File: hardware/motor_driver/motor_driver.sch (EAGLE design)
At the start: 7 parts

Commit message: updating motor driver design 30/07/15
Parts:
- added R1, R2, R3: 10k, adafruit:R-US_R0805
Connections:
- new net !FAULT: R2.1, U$7.!FAULT
- new net !OCTW: R1.1, U$7.!OCTW
- new net 5V: R1.2, R2.2
- new net DTC: R3.2, U$7.DTC
- new net EN_GATE: U$7.EN_GATE
- new net GND: R3.1
- new net N$10: U$7.INH_A
- new net N$11: U$7.INL_A
- new net N$12: U$7.INH_B
- new net N$13: U$7.INL_B
- new net N$14: U$7.INH_C
- new net N$15: U$7.INL_C
- new net N$16: U$7.PVDD2
- new net N$17: U$7.PVDD2(2)
- new net N$18: U$7.VSENSE
- new net N$19: U$7.BST_BK
- new net N$20: U$7.PH1
- new net N$21: U$7.PH2
- new net N$22: U$7.EN_BUCK
- new net N$23: U$7.PWRGD
- new net N$24: U$7.SS_TR
- new net N$25: U$7.RT_CLK
- new net N$26: U$7.COMP
- new net N$27: U$7.CP1
- new net N$28: U$7.CP2
- new net N$29: U$7.SO1
- new net N$30: U$7.SO2
- new net N$31: U$7.SP2
- new net N$32: U$7.SN2
- new net N$33: U$7.DC_CAL
- new net N$34: U$7.REF
- new net N$35: U$7.SP1
- new net N$36: U$7.SN1
- new net N$37: U$7.SL_C
- new net N$38: U$7.GL_C
- new net N$39: U$7.SH_C
- new net N$40: U$7.GH_C
- new net N$41: U$7.BST_C
- new net N$42: U$7.SL_B
- new net N$43: U$7.GL_B
- new net N$44: U$7.SH_B
- new net N$45: U$7.GH_B
- new net N$46: U$7.BST_B
- new net N$47: U$7.SL_A
- new net N$48: U$7.GL_A
- new net N$49: U$7.SA_A
- new net N$5: U$7.M_PWM
- new net N$50: U$7.GH_A
- new net N$51: U$7.BST_A
- new net N$52: U$7.GND
- new net N$53: U$7.AGND
- new net N$54: U$7.DVDD
- new net N$55: U$7.AVDD
- new net N$56: U$7.GVDD
- new net N$57: U$7.PVDD1
- new net N$6: U$7.M_OC
- new net N$7: U$7.GAIN
- new net N$8: U$7.OC_ADJ
- new net N$9: U$7.BIAS

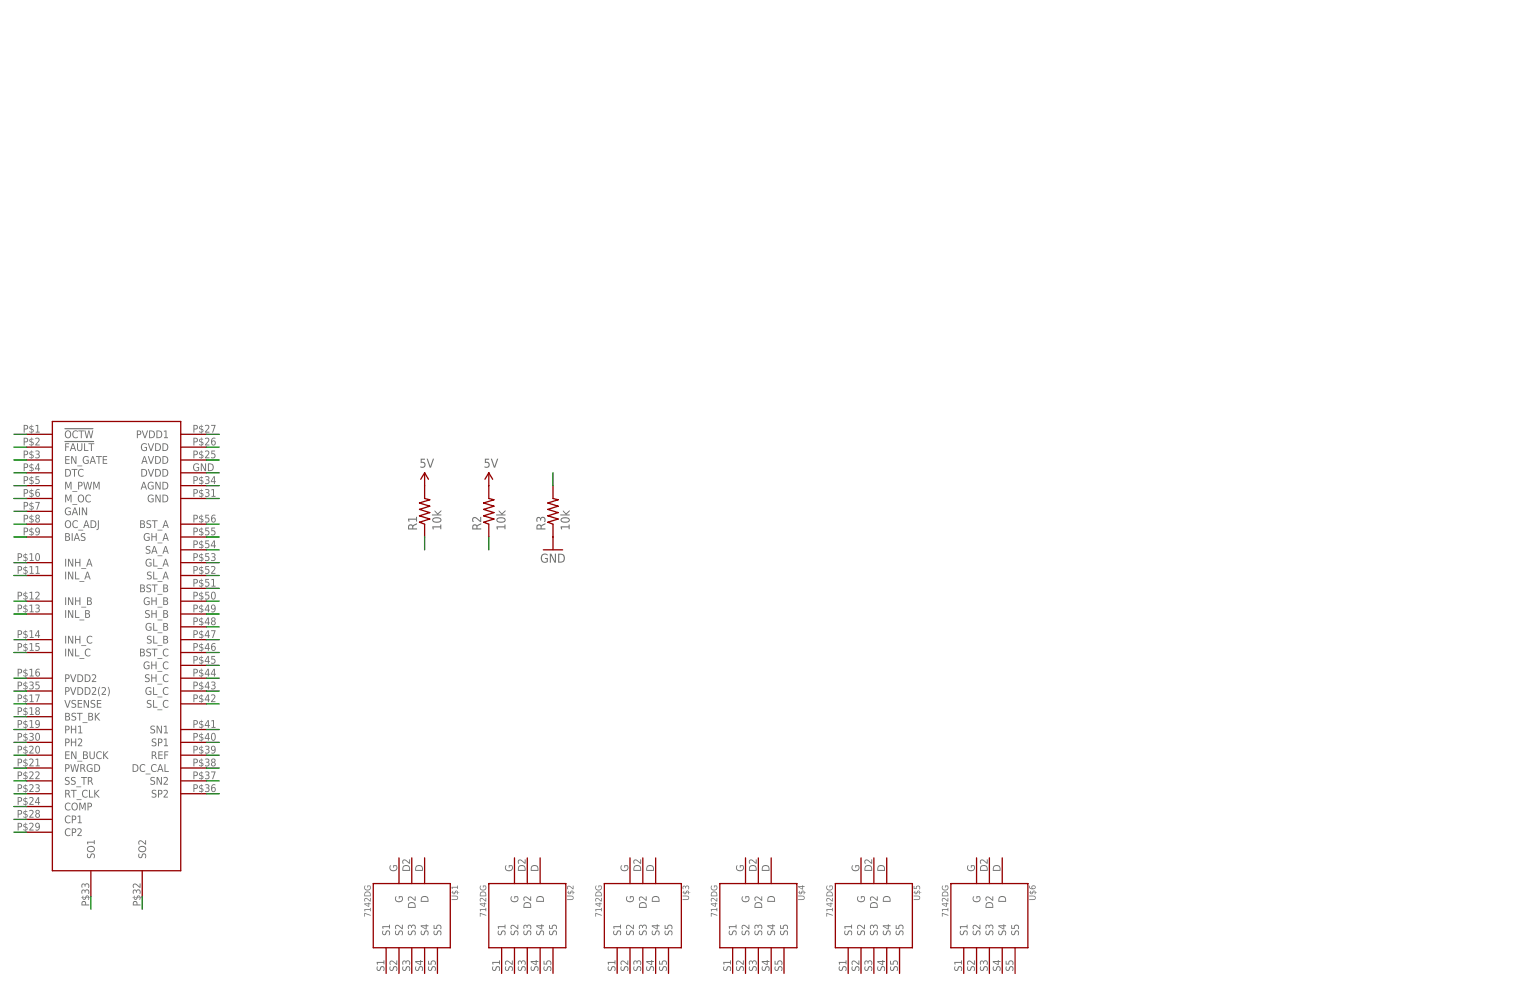
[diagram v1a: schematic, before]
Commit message: Updated motor controller schematic, driver  almost done but components (caps, ind, res) packages still need to be spec'd out
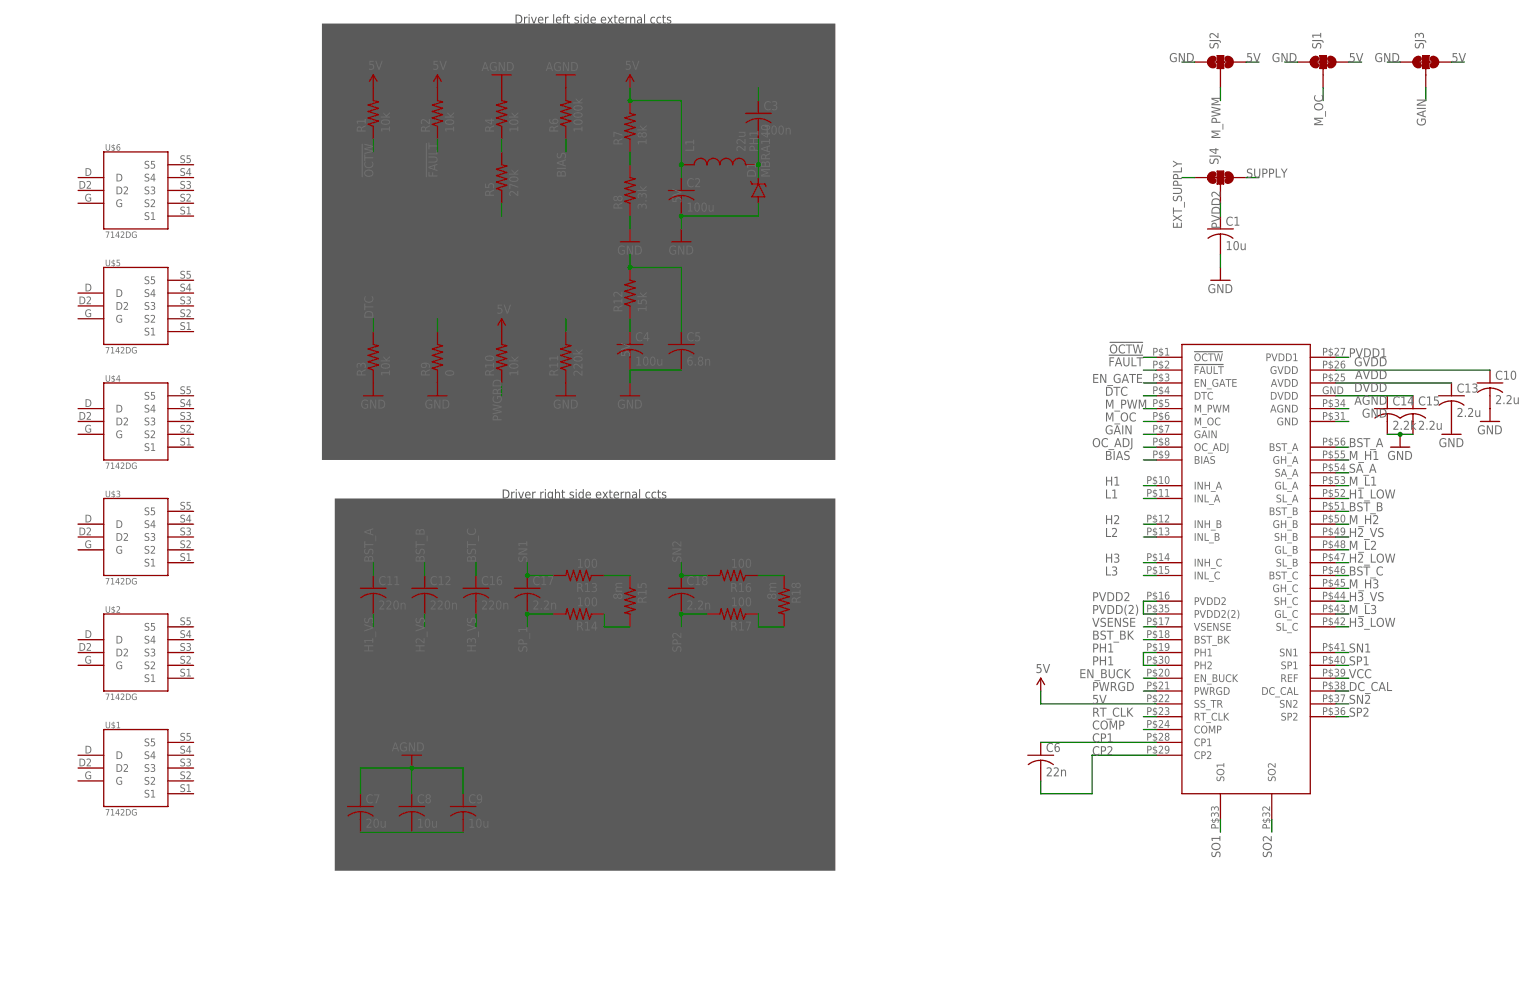
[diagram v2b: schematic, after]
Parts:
- added C1, C8, C9: 10u, adafruit:C-USC1206
- added C10, C13, C15: 2.2u, adafruit:C-USC1206
- added C11, C12, C16: 220n, adafruit:C-USC1206
- added C14: 2.2k, adafruit:C-USC1206
- added C17, C18: 2.2n, adafruit:C-USC1206
- added C2, C4: 100u, adafruit:C-USC1206
- added C3: 100n, adafruit:C-USC1206
- added C5: 6.8n, adafruit:C-USC1206
- added C6: 22n, adafruit:C-USC1206
- added C7: 20u, adafruit:C-USC1206
- added D1: MBRA140, SparkFun-DiscreteSemi:MBRA140
- added L1: 22u, SparkFun-Passives:INDUCTOR30OHM,1.8A
- added R10, R4: 10k, adafruit:R-US_R0805
- added R11: 220k, adafruit:R-US_R0805
- added R12: 15k, adafruit:R-US_R0805
- added R13, R14, R16, R17: 100, adafruit:R-US_R0805
- added R15, R18: 8m, adafruit:R-US_R0805
- added R5: 270k, adafruit:R-US_R0805
- added R6: 1000k, adafruit:R-US_R0805
- added R7: 18k, adafruit:R-US_R0805
- added R8: 3.3k, adafruit:R-US_R0805
- added R9: 0, adafruit:R-US_R0805
- added SJ1, SJ2, SJ3, SJ4: (no value), SparkFun-Passives:JUMPER-PAD-3-NC_BY_TRACE
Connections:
- net N$10 renamed H1
- net N$11 renamed L1
- net N$12 renamed H2
- net N$13 renamed L2
- net N$14 renamed H3
- net N$15 renamed L3
- net N$17 renamed PVDD(2)
- net N$23 renamed PWRGD
- net N$29 renamed SO1
- net N$30 renamed SO2
- net N$33 renamed DC_CAL
- net N$34 renamed VCC
- net N$35 renamed SP1
- net N$38 renamed M_L3
- net N$40 renamed M_H3
- net N$42 renamed H2_LOW
- net N$43 renamed M_L2
- net N$45 renamed M_H2
- net N$48 renamed M_L1
- net N$49 renamed SA_A
- net N$50 renamed M_H1
- removed net N$16: U$7.PVDD2
- removed net N$18: U$7.VSENSE
- removed net N$19: U$7.BST_BK
- removed net N$20: U$7.PH1
- removed net N$21: U$7.PH2
- removed net N$22: U$7.EN_BUCK
- removed net N$24: U$7.SS_TR
- removed net N$25: U$7.RT_CLK
- removed net N$26: U$7.COMP
- removed net N$27: U$7.CP1
- removed net N$28: U$7.CP2
- removed net N$31: U$7.SP2
- removed net N$32: U$7.SN2
- removed net N$36: U$7.SN1
- removed net N$37: U$7.SL_C
- removed net N$39: U$7.SH_C
- removed net N$41: U$7.BST_C
- removed net N$44: U$7.SH_B
- removed net N$46: U$7.BST_B
- removed net N$47: U$7.SL_A
- removed net N$5: U$7.M_PWM
- removed net N$51: U$7.BST_A
- removed net N$52: U$7.GND
- removed net N$53: U$7.AGND
- removed net N$54: U$7.DVDD
- removed net N$55: U$7.AVDD
- removed net N$56: U$7.GVDD
- removed net N$57: U$7.PVDD1
- removed net N$6: U$7.M_OC
- removed net N$7: U$7.GAIN
- removed net N$8: U$7.OC_ADJ
- removed net N$9: U$7.BIAS
- new net AGND: C7.1, C8.1, C9.1, R4.2, R6.2, U$7.AGND
- new net AVDD: C13.1, U$7.AVDD
- new net BIAS: R6.1, U$7.BIAS
- new net BST_A: C11.1, U$7.BST_A
- new net BST_B: C12.1, U$7.BST_B
- new net BST_BK: C3.1, U$7.BST_BK
- new net BST_C: C16.1, U$7.BST_C
- new net COMP: C5.1, R12.2, U$7.COMP
- new net CP1: C6.1, U$7.CP1
- new net CP2: C6.2, U$7.CP2
- new net DVDD: C15.1, R4.1, R5.2, U$7.DVDD
- new net EN_BUCK: R9.2, U$7.EN_BUCK
- new net EXT_SUPPLY: SJ4.1
- new net GAIN: SJ3.2, U$7.GAIN
- new net GVDD: C10.1, U$7.GVDD
- new net H1_LOW: R13.1, R15.1, U$7.SL_A
- new net H1_VS: C11.2
- new net H2_VS: C12.2, U$7.SH_B
- new net H3_LOW: R16.1, R18.1, U$7.SL_C
- new net H3_VS: C16.2, U$7.SH_C
- new net M_OC: SJ1.2, U$7.M_OC
- new net M_PWM: SJ2.2, U$7.M_PWM
- new net N$1: R14.1, R15.2
- new net N$2: R17.1, R18.2
- new net OC_ADJ: R5.1, U$7.OC_ADJ
- new net PH1: C3.2, D1.C, L1.2, U$7.PH1, U$7.PH2
- new net PVDD1: C7.2, C9.2, U$7.PVDD1
- new net PVDD2: C1.1, SJ4.2, U$7.PVDD2
- new net PWGRD: R10.1
- new net RT_CLK: R11.2, U$7.RT_CLK
- new net SN1: C17.1, R13.2, U$7.SN1
- new net SN2: C18.1, R16.2, U$7.SN2
- new net SP2: C18.2, R17.2, U$7.SP2
- new net SP_1: C17.2, R14.2
- new net SUPPLY: SJ4.3
- new net VSENSE: R7.1, R8.2, U$7.VSENSE
- net 5V: now also C2.1, C4.1, L1.1, R10.2, R12.1, R7.2, SJ1.3, SJ2.3, SJ3.3, U$7.SS_TR
- net GND: now also C1.2, C10.2, C13.2, C14.2, C15.2, C2.2, C4.2, C5.2, D1.A, R11.1, R8.1, R9.1, SJ1.1, SJ2.1, SJ3.1, U$7.GND
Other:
- note added: "Driver left side external ccts"
- note added: "Driver right side external ccts"
- moved on the sheet: R1, R2, R3, U$1, U$2, U$3, U$4, U$5, U$6

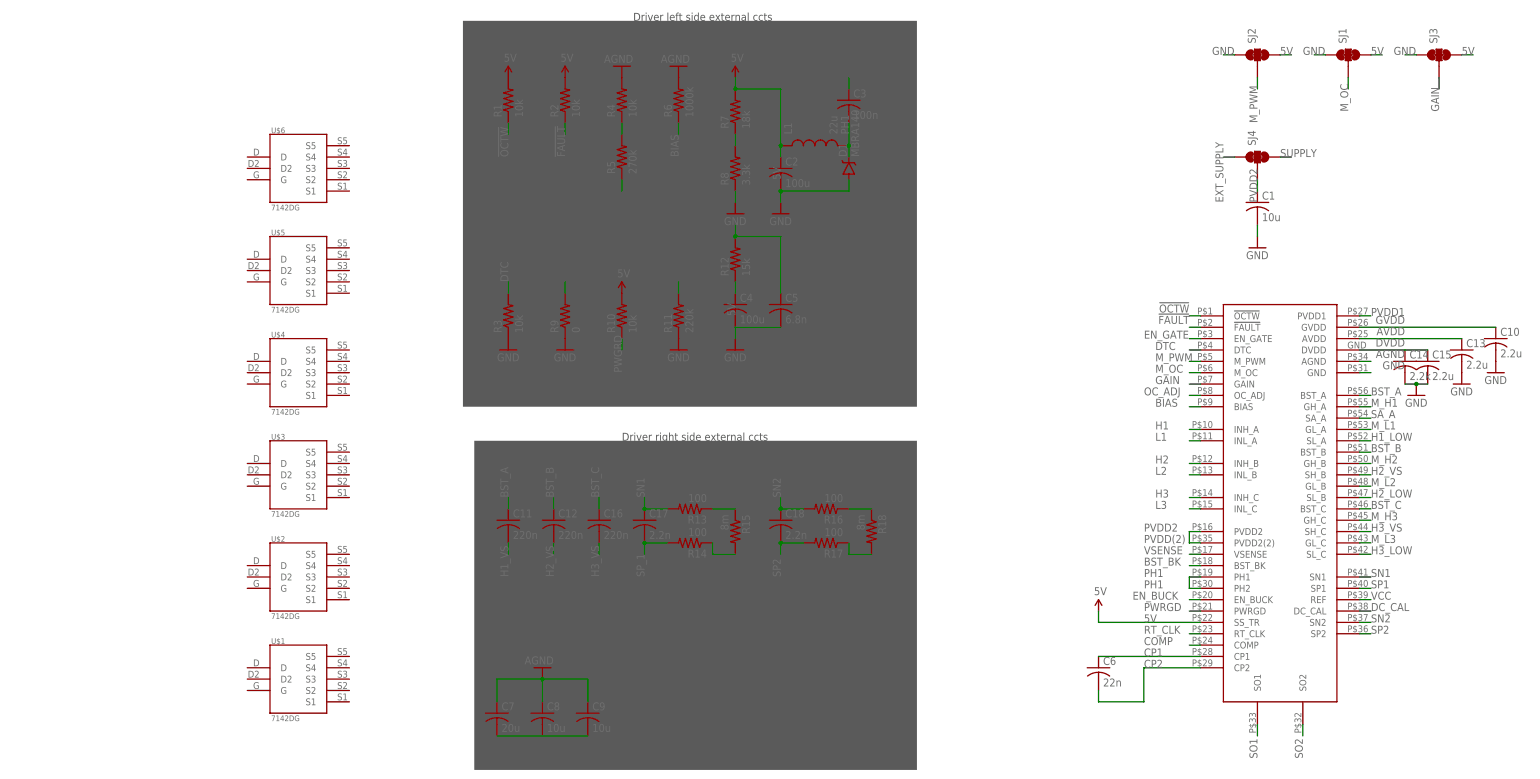
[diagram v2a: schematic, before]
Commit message: Finished driver and MOSFET's external connections. Package choices still need to be reviewed
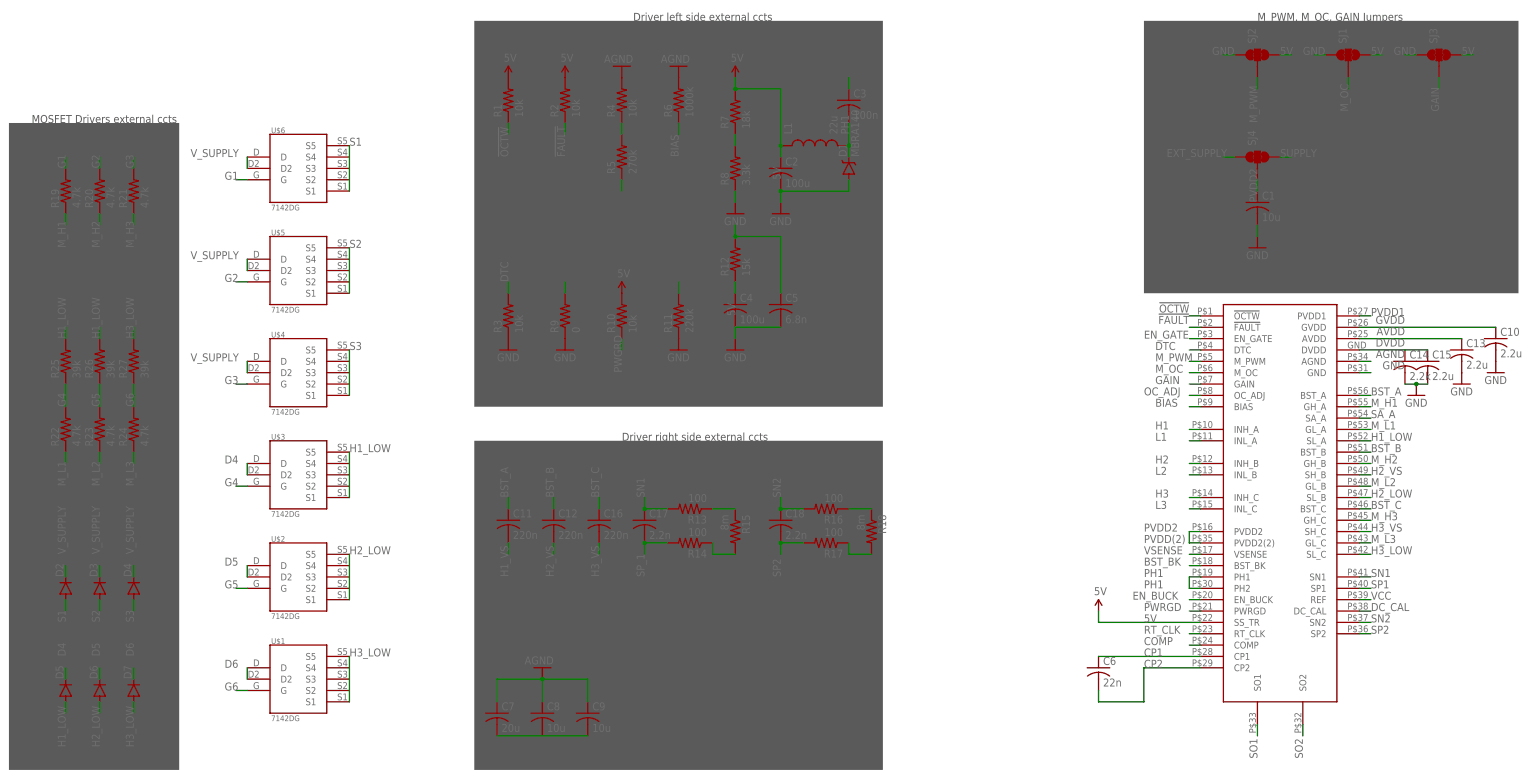
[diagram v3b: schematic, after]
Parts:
- added D2, D3, D4, D5, D6, D7: (no value), SparkFun-DiscreteSemi:DIODESOD123
- added R19, R20, R21, R22, R23, R24: 4.7k, adafruit:R-US_R2512
- added R25, R26, R27: 39k, adafruit:R-US_R2512
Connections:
- new net D4: D5.C, U$3.D, U$3.D2
- new net D5: D6.C, U$2.D, U$2.D2
- new net D6: D7.C, U$1.D, U$1.D2
- new net G1: R19.2, U$6.G
- new net G2: R20.2, U$5.G
- new net G3: R21.2, U$4.G
- new net G4: R22.2, U$3.G
- new net G5: R23.2, U$2.G
- new net G6: R24.2, U$1.G
- new net M_L4: R27.1
- new net M_L5: R26.1
- new net M_L6: R25.1
- new net S1: D2.A, U$6.S1, U$6.S5
- new net S2: D3.A, U$5.S1, U$5.S5
- new net S3: D4.A, U$4.S1, U$4.S5
- new net V_SUPPLY: D2.C, D3.C, D4.C, U$4.D, U$4.D2, U$5.D, U$5.D2, U$6.D, U$6.D2
- net H1_LOW: now also D5.A, R25.2, R26.2, U$3.S1, U$3.S5
- net H2_LOW: now also D6.A, U$2.S1, U$2.S5
- net H3_LOW: now also D7.A, R27.2, U$1.S1, U$1.S5
- net M_H1: now also R19.1
- net M_H2: now also R20.1
- net M_H3: now also R21.1
- net M_L1: now also R22.1
- net M_L2: now also R23.1
- net M_L3: now also R24.1
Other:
- note added: "MOSFET Drivers external ccts"
- note added: "M_PWM, M_OC, GAIN Jumpers"
